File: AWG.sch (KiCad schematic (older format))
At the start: 91 parts, among them J1001 Conn_01x03, J1002 Conn_01x05, J1003 Conn_01x06, J1004 Conn_01x06, J1005 Conn_01x01, J1006 Conn_01x01, J1007 Conn_01x01, J1008 Conn_01x01, J1009 Conn_01x01, J1010 Conn_01x01, J1011 Conn_01x01, J1012 Conn_01x01, J2 Conn afficheur, J5 SMA, J6 SMA, J7 BNC, Q1001 NTE2633, Q1002 NTE2634, SW1 Reset, SW2 Encodeur sur façade, SW3 Next, SW4 Previous, SW5 AC/DC, SW6 50R/Low Z, U1 Pico, U1001 L7812, U1002 L7912, U1003 L7805, U1004 L7905, U3 AD8055ARZ

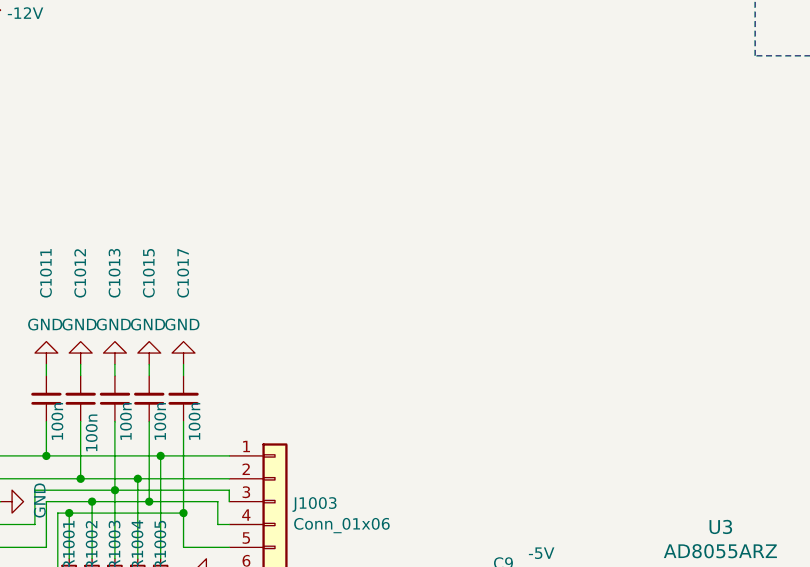
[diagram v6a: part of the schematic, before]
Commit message: auxiliary power connector added
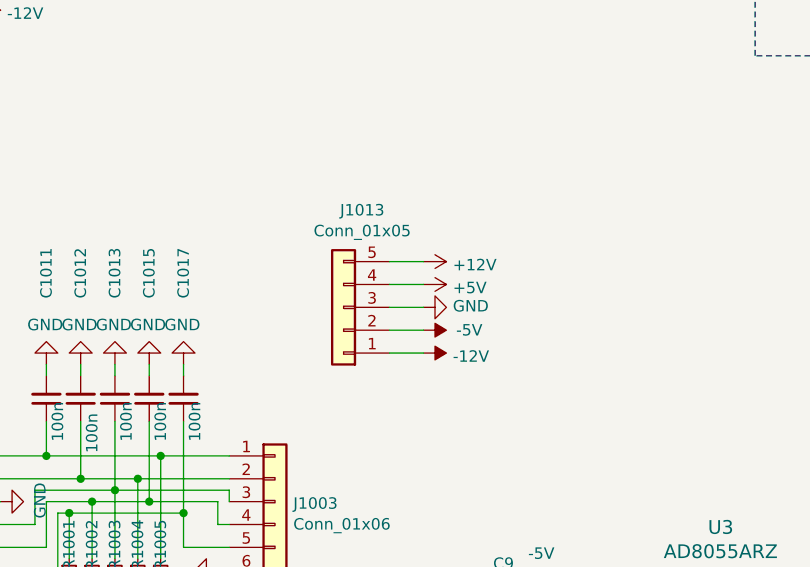
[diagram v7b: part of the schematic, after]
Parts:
- added J1013: Conn_01x05, Connector_Molex:Molex_KK-254_AE-6410-05A_1x05_P2.54mm_Vertical, symbol Connector_Generic:Conn_01x05
- D1, D2: footprint Diode_SMD:D_MiniMELF_Handsoldering -> Diode_SMD:D_MicroMELF_Handsoldering
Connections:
- net +12V: now also J1013.5 (Pin_5)
- net +5V: now also J1013.4 (Pin_4)
- net -12V: now also J1013.1 (Pin_1)
- net -5V: now also J1013.2 (Pin_2)
- net GND: now also J1013.3 (Pin_3)
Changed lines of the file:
@@
 F 0 "D2" V 8896 4830 50  0000 R CNN
 F 1 "4148" V 8805 4830 50  0000 R CNN
-F 2 "Diode_SMD:D_MiniMELF_Handsoldering" V 8850 4900 50  0001 C CNN
+F 2 "Diode_SMD:D_MicroMELF_Handsoldering" V 8850 4900 50  0001 C CNN
 F 3 "~" V 8850 4900 50  0001 C CNN
 	1    8850 4900
@@
 F 0 "D1" V 8896 4230 50  0000 R CNN
 F 1 "4148" V 8805 4230 50  0000 R CNN
-F 2 "Diode_SMD:D_MiniMELF_Handsoldering" V 8850 4300 50  0001 C CNN
+F 2 "Diode_SMD:D_MicroMELF_Handsoldering" V 8850 4300 50  0001 C CNN
 F 3 "~" V 8850 4300 50  0001 C CNN
 	1    8850 4300
@@
 	-1   0    0    1
 $EndComp
+$Comp
+L power:+5V #PWR01006
+U 1 1 61B7EEE6
+P 6350 2900
+F 0 "#PWR01006" H 6350 2750 50  0001 C CNN
+F 1 "+5V" V 6365 3028 50  0000 L CNN
+F 2 "" H 6350 2900 50  0001 C CNN
+F 3 "" H 6350 2900 50  0001 C CNN
+	1    6350 2900
+	0    1    1    0
+$EndComp
+Wire Wire Line
+	6200 2800 6350 2800
+Wire Wire Line
+	6200 3000 6350 3000
+Wire Wire Line
+	6200 2900 6350 2900
+Wire Wire Line
+	6200 3200 6350 3200
+$Comp
+L power:-12V #PWR01009
+U 1 1 61B7EEF4
+P 6350 3200
+F 0 "#PWR01009" H 6350 3300 50  0001 C CNN
+F 1 "-12V" V 6365 3328 50  0000 L CNN
+F 2 "" H 6350 3200 50  0001 C CNN
+F 3 "" H 6350 3200 50  0001 C CNN
+	1    6350 3200
+	0    1    1    0
+$EndComp
+$Comp
+L power:+12V #PWR01005
+U 1 1 61B7EEFE
+P 6350 2800
+F 0 "#PWR01005" H 6350 2650 50  0001 C CNN
+F 1 "+12V" V 6365 2928 50  0000 L CNN
+F 2 "" H 6350 2800 50  0001 C CNN
+F 3 "" H 6350 2800 50  0001 C CNN
+	1    6350 2800
+	0    1    1    0
+$EndComp
+$Comp
+L power:GND #PWR01007
+U 1 1 61B7EF08
+P 6350 3000
+F 0 "#PWR01007" H 6350 2750 50  0001 C CNN
+F 1 "GND" V 6355 2872 50  0000 R CNN
+F 2 "" H 6350 3000 50  0001 C CNN
+F 3 "" H 6350 3000 50  0001 C CNN
+	1    6350 3000
+	0    -1   -1   0
+$EndComp
+$Comp
+L Connector_Generic:Conn_01x05 J1013
+U 1 1 61B7EF12
+P 6000 3000
+F 0 "J1013" H 5918 2575 50  0000 C CNN
+F 1 "Conn_01x05" H 5918 2666 50  0000 C CNN
+F 2 "Connector_Molex:Molex_KK-254_AE-6410-05A_1x05_P2.54mm_Vertical" H 6000 3000 50  0001 C CNN
+F 3 "~" H 6000 3000 50  0001 C CNN
+	1    6000 3000
+	-1   0    0    1
+$EndComp
+Wire Wire Line
+	6200 3100 6350 3100
+$Comp
+L power:-5V #PWR01008
+U 1 1 61B7EF1D
+P 6350 3100
+F 0 "#PWR01008" H 6350 3200 50  0001 C CNN
+F 1 "-5V" V 6350 3300 50  0000 C CNN
+F 2 "" H 6350 3100 50  0001 C CNN
+F 3 "" H 6350 3100 50  0001 C CNN
+	1    6350 3100
+	0    1    1    0
+$EndComp
 $EndSCHEMATC

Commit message: 1mf non polar cap added
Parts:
- C6: footprint (none) -> Capacitor_THT:C_Radial_D10.0mm_H16.0mm_P5.00mm
- C7: footprint Capacitor_SMD:C_0805_2012Metric -> Capacitor_SMD:C_0805_2012Metric_Pad1.18x1.45mm_HandSolder
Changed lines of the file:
@@
 F 0 "C6" V 5821 4450 50  0000 C CNN
 F 1 "1mF" V 5912 4450 50  0000 C CNN
-F 2 "" H 6050 4450 50  0001 C CNN
+F 2 "Capacitor_THT:C_Radial_D10.0mm_H16.0mm_P5.00mm" H 6050 4450 50  0001 C CNN
 F 3 "~" H 6050 4450 50  0001 C CNN
 	1    6050 4450
@@
 F 0 "C7" H 6350 5700 50  0000 L CNN
 F 1 "3.3p" H 6300 5450 50  0000 L CNN
-F 2 "Capacitor_SMD:C_0805_2012Metric" H 6400 5550 50  0001 C CNN
+F 2 "Capacitor_SMD:C_0805_2012Metric_Pad1.18x1.45mm_HandSolder" H 6400 5550 50  0001 C CNN
 F 3 "~" H 6400 5550 50  0001 C CNN
 	1    6400 5550
